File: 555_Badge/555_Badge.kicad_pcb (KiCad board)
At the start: 2 copper layers, 15 parts, among them Q1 2N3904, U1 7555

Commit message: Partial board
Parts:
- moved R4 63.4 mm to (219.1, 99.1), turned to 270 degrees
- moved R1 54.3 mm to (194.9, 99.1), turned to 270 degrees
- moved S1 50.5 mm to (181.6, 104.8), turned to 90 degrees
- moved R5 48.1 mm to (201.3, 111.1)
- moved R6 45.6 mm to (200.7, 99.1), turned to 270 degrees
- moved R3 45.4 mm to (212.1, 99.1), turned to 270 degrees
- moved R7 39.1 mm to (206.4, 99.1), turned to 270 degrees
- moved C2 38.9 mm to (202.6, 118.7)
- moved BAT1 36.5 mm to (163.8, 117.5), turned to 90 degrees
- moved U1 34.6 mm to (184.2, 117.5)
- moved R2 33.4 mm to (189.2, 99.1), turned to 270 degrees
- moved Q1 29.9 mm to (194.3, 113.7), turned to 90 degrees
- moved C1 29.6 mm to (194.3, 121.3)
- moved D1 29.4 mm to (201.9, 93.3), turned to 90 degrees
- moved D2 26.5 mm to (191.1, 93.3), turned to 90 degrees
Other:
- net class Default: clearance 0.2 -> 0.254; trace_width 0.25 -> 0.254; via_dia 0.8 -> 0.762; via_drill 0.4 -> 0.381
- rule pad_to_mask_clearance: 0 -> 0.0508
- rule trace_clearance: 0.2 -> 0.254
- rule trace_min: 0.2 -> 0.1524
- rule via_min_drill: 0.3 -> 0.3302
- rule via_min_size: 0.4 -> 0.6858

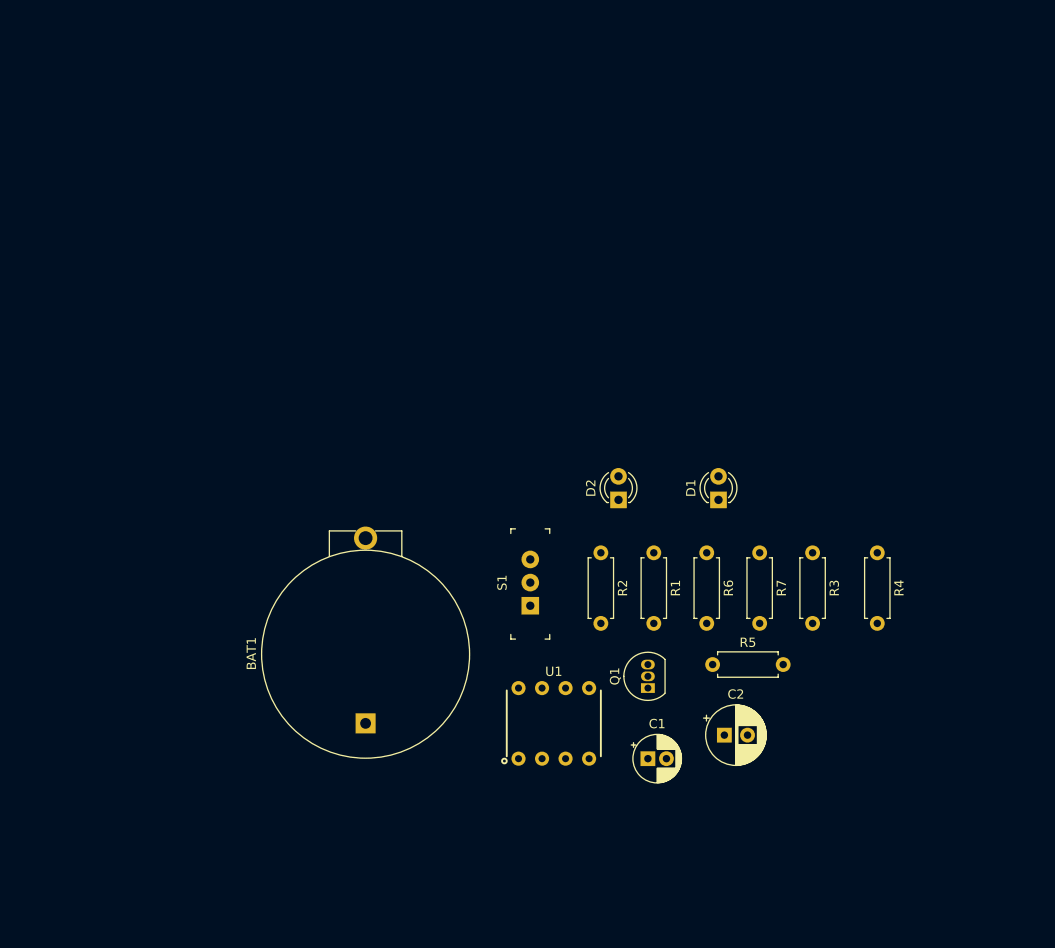
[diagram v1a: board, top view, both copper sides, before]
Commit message: Start board outline
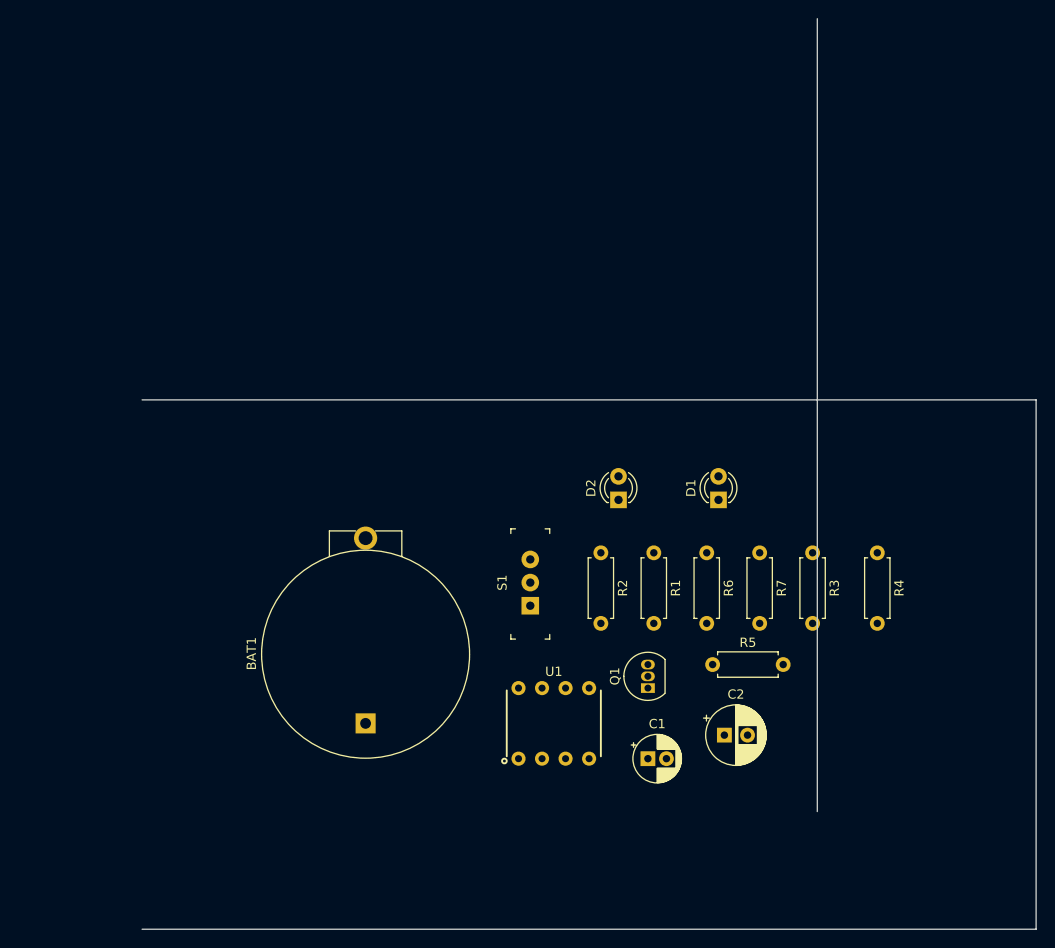
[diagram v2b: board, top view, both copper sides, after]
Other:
- board outline added: 96.5 x 98.3 mm

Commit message: Place completed
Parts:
- moved D1 57.4 mm to (147.6, 74.9)
- moved R4 41.3 mm to (177.8, 100.3)
- moved R3 38.1 mm to (174.0, 100.3)
- moved R7 36.2 mm to (170.2, 100.3)
- moved D2 35.9 mm to (160.3, 74.9)
- moved R6 34.3 mm to (166.4, 100.3)
- moved R1 32.4 mm to (162.6, 100.3)
- moved R2 30.5 mm to (158.8, 100.3)
- moved C2 29.9 mm to (172.7, 119.4)
- moved R5 29.9 mm to (171.4, 111.8)
- moved C1 29.3 mm to (165.1, 119.4)
- moved S1 28.0 mm to (153.7, 106.7)
- moved Q1 27.9 mm to (166.4, 114.3)
- moved U1 26.7 mm to (157.5, 118.1)
- moved BAT1 24.2 mm to (139.7, 118.7)
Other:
- board size 96.5 x 98.3 mm -> 53.8 x 85.6 mm

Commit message: Net01 added
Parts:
- moved C2 3.70 mm to (176.3, 118.4), turned to 270 degrees
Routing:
- net Net-(C2-Pad1): track 0.00 -> 7.76 mm
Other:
- net class Net01 added: clearance 0.254, trace_width 0.254, via_dia 0.762, via_drill 0.381
